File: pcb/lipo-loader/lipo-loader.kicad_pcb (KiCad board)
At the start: 2 copper layers, 9 parts, among them J1 IN_VCC, J2 IN_GND, J3 TP_BATT_VCC, J4 TP_BATT_GND, J5 BATT

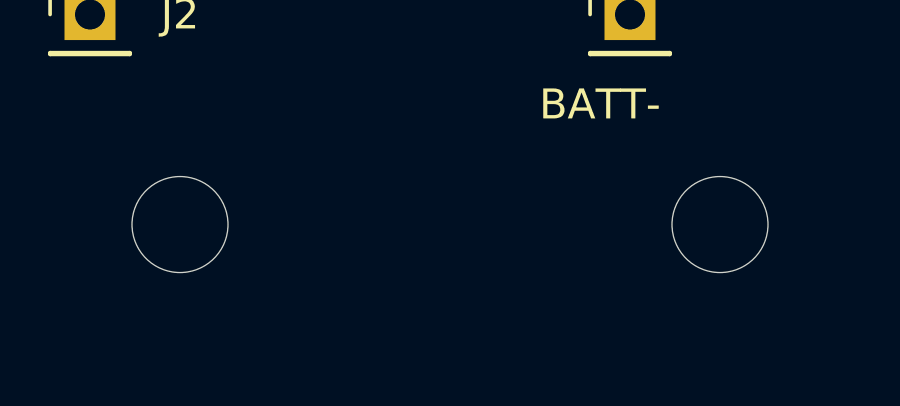
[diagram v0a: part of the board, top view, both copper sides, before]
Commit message: Final Update of LiPO Loader for the sensor
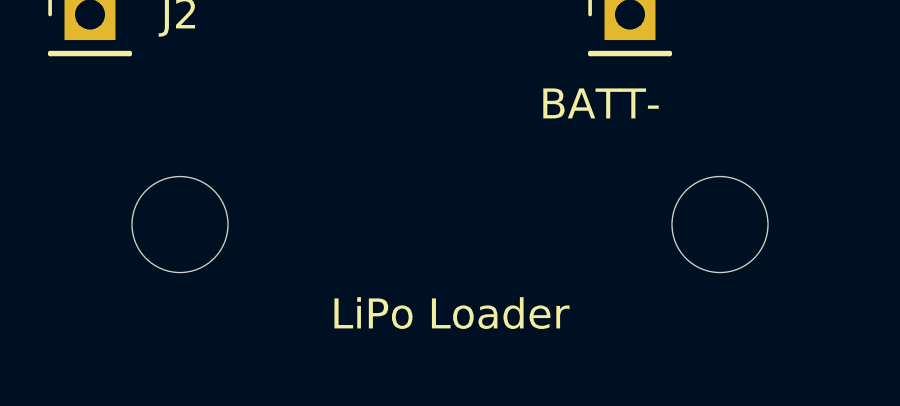
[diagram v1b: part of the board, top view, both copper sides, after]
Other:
- board text added: "JLCJLCJLCJLC"
- board text added: "LiPo Loader"

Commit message: update lipo loader
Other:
- board outline added: 31 x 38 mm
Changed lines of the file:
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@@
   (general
     (thickness 1.6)
-    (drawings 12)
+    (drawings 10)
     (tracks 4)
     (zones 0)
@@
       (layerselection 0x010fc_ffffffff)
       (usegerberextensions false)
-      (usegerberattributes true)
-      (usegerberadvancedattributes true)
-      (creategerberjobfile true)
+      (usegerberattributes false)
+      (usegerberadvancedattributes false)
+      (creategerberjobfile false)
       (excludeedgelayer true)
       (linewidth 0.100000)
@@
       (psa4output false)
       (plotreference true)
-      (plotvalue true)
+      (plotvalue false)
       (plotinvisibletext false)
-      (padsonsilk false)
+      (padsonsilk true)
       (subtractmaskfromsilk false)
-      (outputformat 4)
+      (outputformat 1)
       (mirror false)
       (drillshape 0)
       (scaleselection 1)
-      (outputdirectory "/tmp/"))
+      (outputdirectory "/tmp/lipo-loader"))
   )
   (net 0 "")
@@
     (pad 1 np_thru_hole circle (at 0 0) (size 3.2 3.2) (drill 3.2) (layers *.Cu *.Mask))
   )
+  (gr_line (start 123 78) (end 154 78) (layer Edge.Cuts) (width 0.05))
+  (gr_line (start 123 116) (end 123 78) (layer Edge.Cuts) (width 0.05))
+  (gr_line (start 154 116) (end 123 116) (layer Edge.Cuts) (width 0.05))
+  (gr_line (start 154 78) (end 154 116) (layer Edge.Cuts) (width 0.05))
   (gr_text JLCJLCJLCJLC (at 137 97) (layer B.SilkS)
     (effects (font (size 1 1) (thickness 0.15)) (justify mirror))
@@
     (effects (font (size 1 1) (thickness 0.15)))
   )
-  (gr_line (start 123 78) (end 146 78) (layer Eco2.User) (width 0.15))
-  (gr_line (start 123 103) (end 123 78) (layer Eco2.User) (width 0.15))
-  (gr_line (start 123 116) (end 123 103) (layer Eco2.User) (width 0.15))
-  (gr_line (start 154 116) (end 123 116) (layer Eco2.User) (width 0.15))
-  (gr_line (start 154 78) (end 154 116) (layer Eco2.User) (width 0.15))
-  (gr_line (start 146 78) (end 154 78) (layer Eco2.User) (width 0.15))
   (segment (start 144 90) (end 149 95) (width 0.25) (layer B.Cu) (net 3))
   (segment (start 143 90) (end 144 90) (width 0.25) (layer B.Cu) (net 3))
